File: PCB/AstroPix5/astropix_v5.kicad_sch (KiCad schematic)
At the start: 41 parts, among them J1 HBOut, J12 Measures_Analog, J13 pcie_GECCO, J14 Bias, J2 Conn_01x05, J3 SPI_left, J4 HBOut, J5 HBOut, J7 HV_in_external, J8 Conn_01x03, U2 AstroPix5_split_powerring

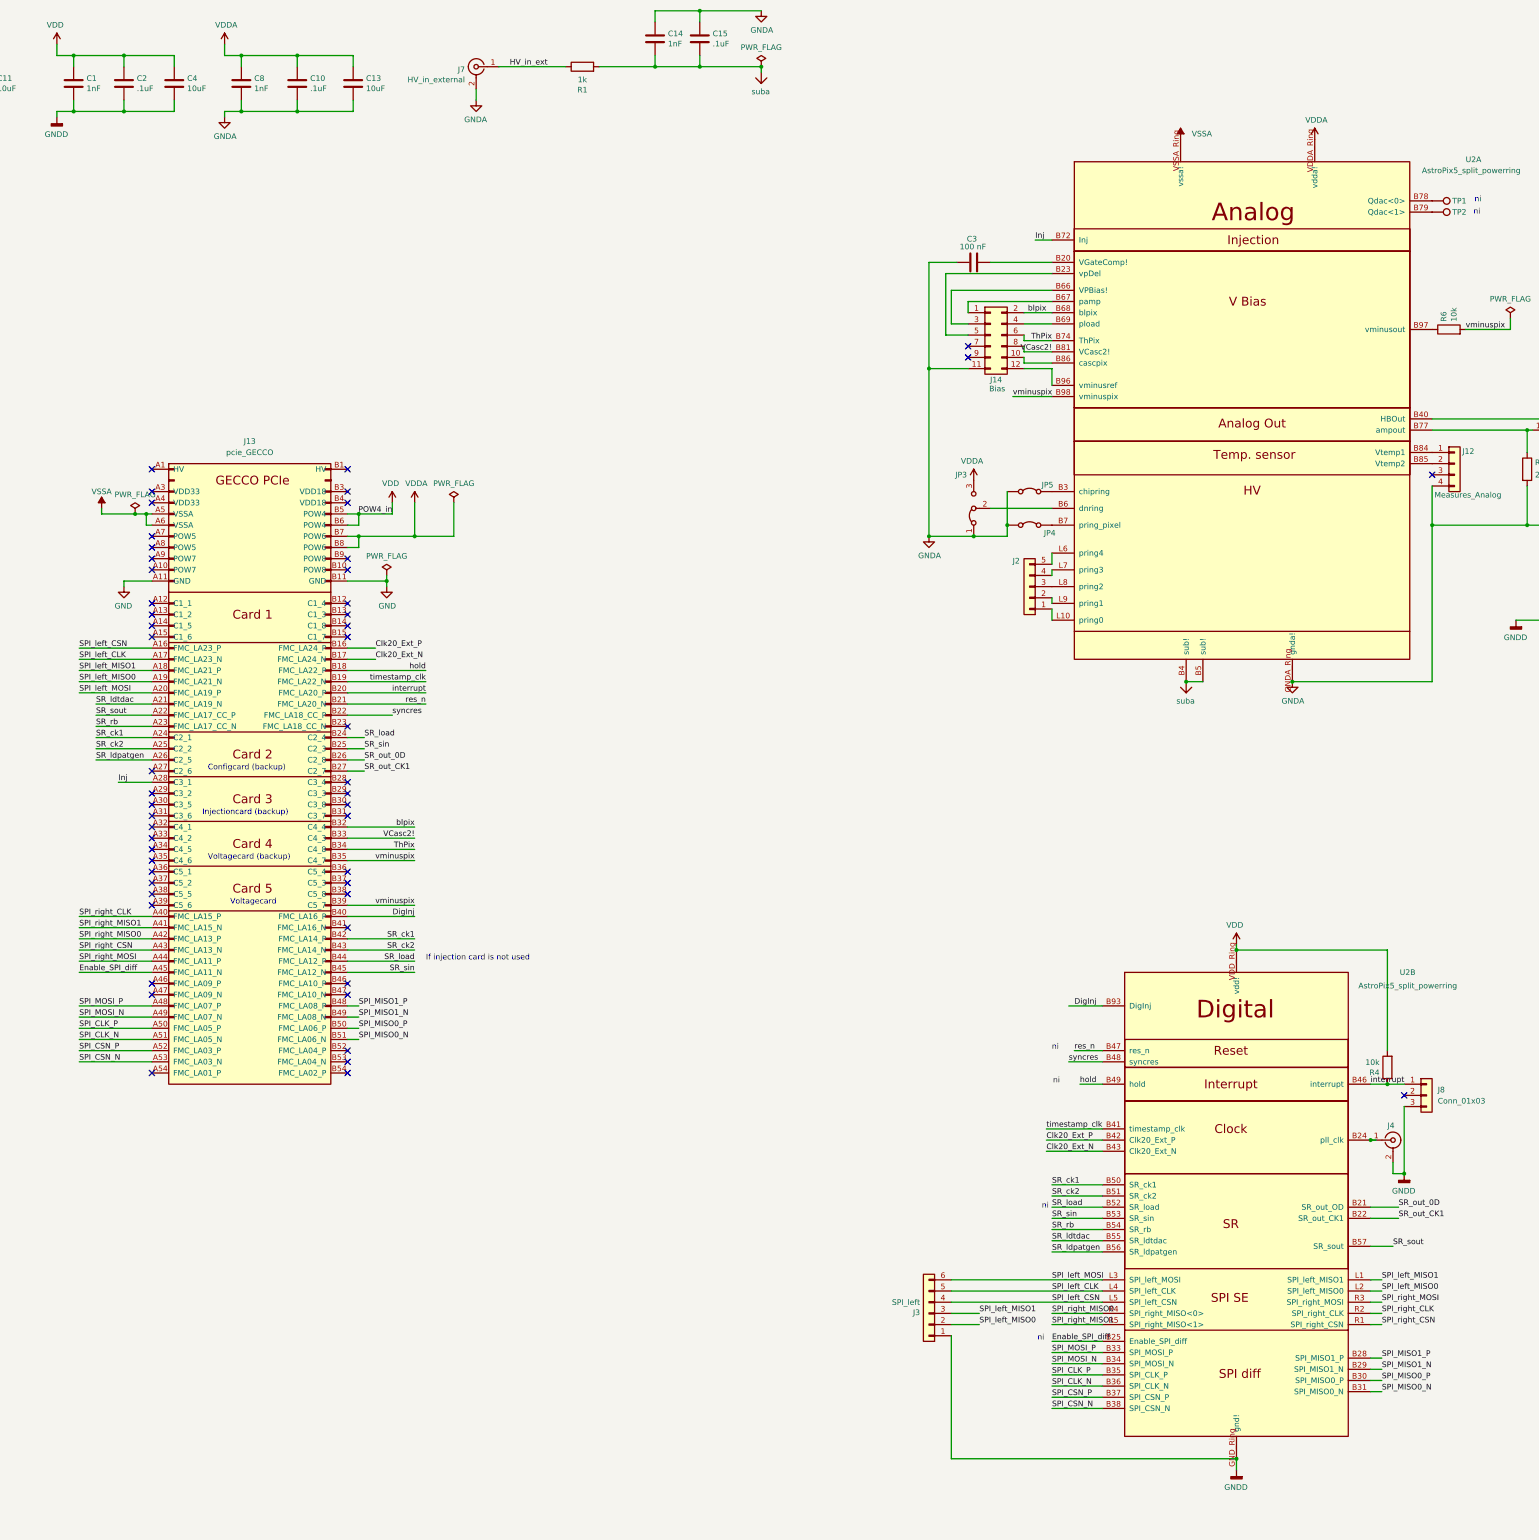
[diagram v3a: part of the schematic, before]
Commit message: Layout change schematic pcie change
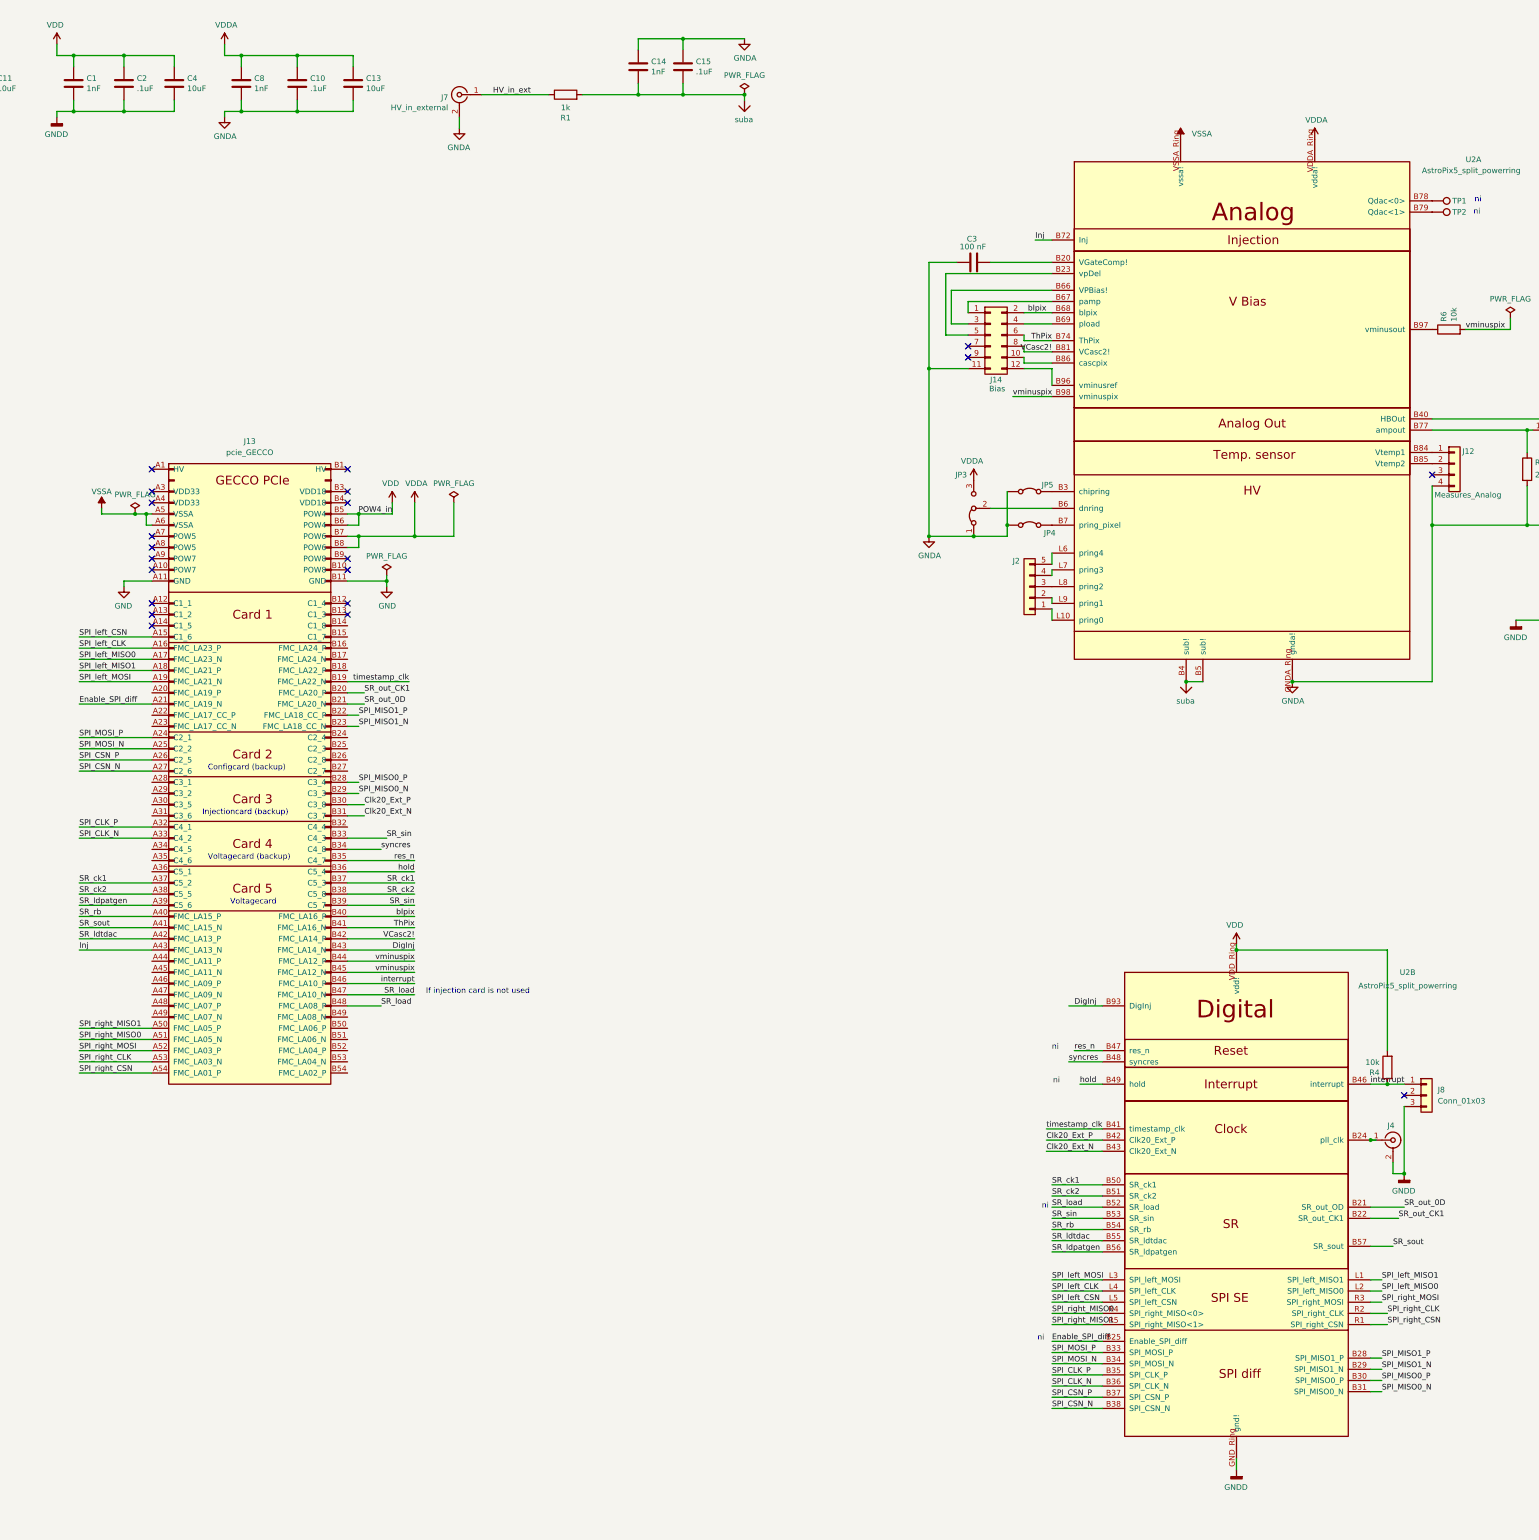
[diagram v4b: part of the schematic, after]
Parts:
- removed J3: SPI_left, Connector_PinHeader_2.54mm:PinHeader_1x06_P2.54mm_Vertical, symbol Connector_Generic:Conn_01x06
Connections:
- net Clk20_Ext_N: now also J13.B31 (C3_7); no longer J13.B17 (FMC_LA24_N)
- net Clk20_Ext_P: now also J13.B30 (C3_8); no longer J13.B16 (FMC_LA24_P)
- net DigInj: now also J13.B43 (FMC_LA14_N); no longer J13.B40 (FMC_LA16_P)
- net Enable_SPI_diff: now also J13.A21 (FMC_LA19_N); no longer J13.A45 (FMC_LA11_N)
- net Inj: now also J13.A43 (FMC_LA13_N); no longer J13.A28 (C3_1)
- net SPI_CLK_N: now also J13.A33 (C4_2); no longer J13.A51 (FMC_LA05_N)
- net SPI_CLK_P: now also J13.A32 (C4_1); no longer J13.A50 (FMC_LA05_P)
- net SPI_CSN_N: now also J13.A27 (C2_6); no longer J13.A53 (FMC_LA03_N)
- net SPI_CSN_P: now also J13.A26 (C2_5); no longer J13.A52 (FMC_LA03_P)
- net SPI_MISO0_N: now also J13.B29 (C3_3); no longer J13.B51 (FMC_LA06_N)
- net SPI_MISO0_P: now also J13.B28 (C3_4); no longer J13.B50 (FMC_LA06_P)
- net SPI_MISO1_N: now also J13.B23 (FMC_LA18_CC_N); no longer J13.B49 (FMC_LA08_N)
- net SPI_MISO1_P: now also J13.B22 (FMC_LA18_CC_P); no longer J13.B48 (FMC_LA08_P)
- net SPI_MOSI_N: now also J13.A25 (C2_2); no longer J13.A49 (FMC_LA07_N)
- net SPI_MOSI_P: now also J13.A24 (C2_1); no longer J13.A48 (FMC_LA07_P)
- net SPI_left_CLK: now also J13.A16 (FMC_LA23_P); no longer J13.A17 (FMC_LA23_N)
- net SPI_left_CSN: now also J13.A15 (C1_6); no longer J13.A16 (FMC_LA23_P)
- net SPI_left_MISO0: now also J13.A17 (FMC_LA23_N); no longer J13.A19 (FMC_LA21_N)
- net SPI_left_MOSI: now also J13.A19 (FMC_LA21_N); no longer J13.A20 (FMC_LA19_P)
- net SPI_right_CLK: now also J13.A53 (FMC_LA03_N); no longer J13.A40 (FMC_LA15_P)
- net SPI_right_CSN: now also J13.A54 (FMC_LA01_P); no longer J13.A43 (FMC_LA13_N)
- net SPI_right_MISO0: now also J13.A51 (FMC_LA05_N); no longer J13.A42 (FMC_LA13_P)
- net SPI_right_MISO1: now also J13.A50 (FMC_LA05_P); no longer J13.A41 (FMC_LA15_N)
- net SPI_right_MOSI: now also J13.A52 (FMC_LA03_P); no longer J13.A44 (FMC_LA11_P)
- net SR_ck1: now also J13.A37 (C5_2), J13.B37 (C5_3); no longer J13.A24 (C2_1), J13.B42 (FMC_LA14_P)
- net SR_ck2: now also J13.A38 (C5_5), J13.B38 (C5_8); no longer J13.A25 (C2_2), J13.B43 (FMC_LA14_N)
- net SR_ldpatgen: now also J13.A39 (C5_6); no longer J13.A26 (C2_5)
- net SR_ldtdac: now also J13.A42 (FMC_LA13_P); no longer J13.A21 (FMC_LA19_N)
- net SR_load: now also J13.B47 (FMC_LA10_N), J13.B48 (FMC_LA08_P); no longer J13.B24 (C2_4), J13.B44 (FMC_LA12_P)
- net SR_out_0D: now also J13.B21 (FMC_LA20_N); no longer J13.B26 (C2_8)
- net SR_out_CK1: now also J13.B20 (FMC_LA20_P); no longer J13.B27 (C2_7)
- net SR_rb: now also J13.A40 (FMC_LA15_P); no longer J13.A23 (FMC_LA17_CC_N)
- net SR_sin: now also J13.B33 (C4_3), J13.B39 (C5_7); no longer J13.B25 (C2_3), J13.B45 (FMC_LA12_N)
- net SR_sout: now also J13.A41 (FMC_LA15_N); no longer J13.A22 (FMC_LA17_CC_P)
- net ThPix: now also J13.B41 (FMC_LA16_N); no longer J13.B34 (C4_8)
- net VCasc2!: now also J13.B42 (FMC_LA14_P); no longer J13.B33 (C4_3)
- net blpix: now also J13.B40 (FMC_LA16_P); no longer J13.B32 (C4_4)
- net hold: now also J13.B36 (C5_4); no longer J13.B18 (FMC_LA22_P)
- net interrupt: now also J13.B46 (FMC_LA10_P); no longer J13.B20 (FMC_LA20_P)
- net res_n: now also J13.B35 (C4_7); no longer J13.B21 (FMC_LA20_N)
- net syncres: now also J13.B34 (C4_8); no longer J13.B22 (FMC_LA18_CC_P)
- net vminuspix: now also J13.B44 (FMC_LA12_P), J13.B45 (FMC_LA12_N); no longer J13.B35 (C4_7), J13.B39 (C5_7)
- no-connect marks 53 -> 21
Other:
- moved on the sheet: C14, C15, J7, R1
